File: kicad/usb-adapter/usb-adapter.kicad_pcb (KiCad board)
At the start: 2 copper layers, 17.2 x 40 mm, 3 parts, among them J1 USB-A plug, port A, J2 USB-A plug, port B, J3 To main board

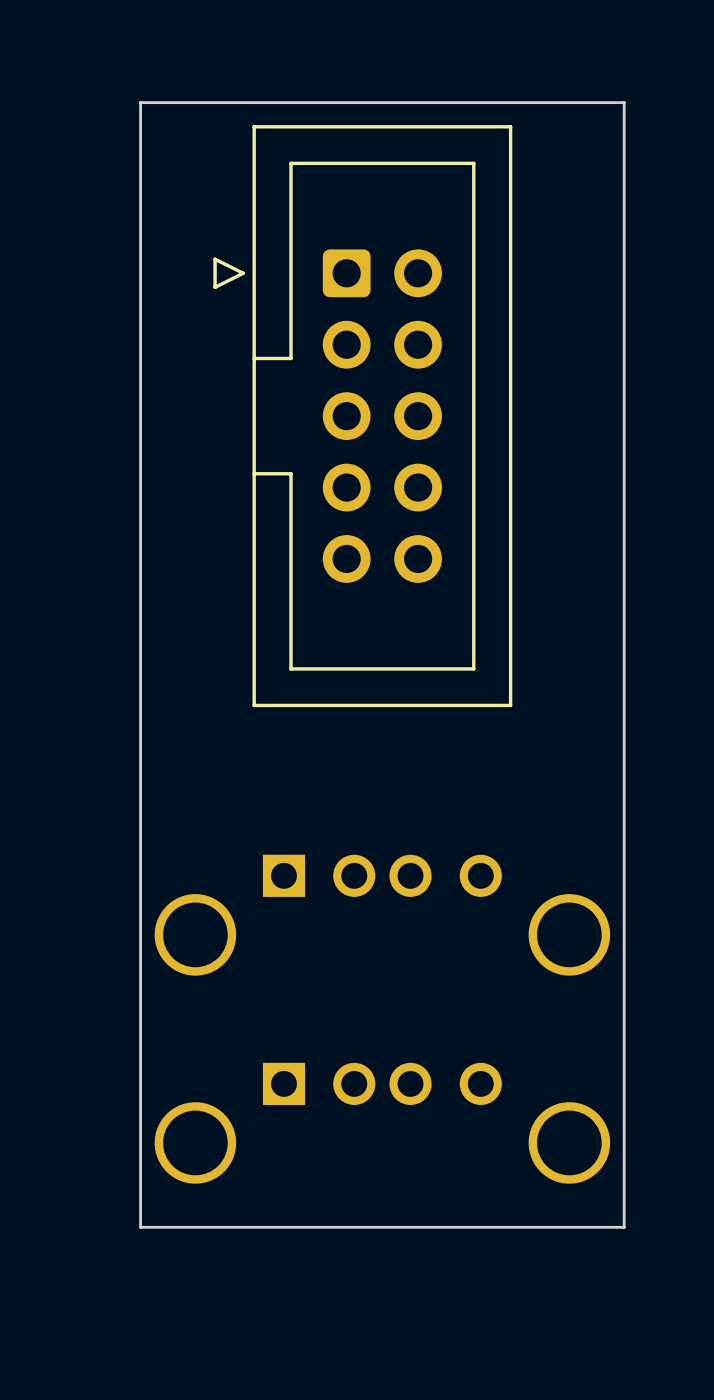
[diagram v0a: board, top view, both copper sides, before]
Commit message: USB adapter: port heights from the Pi 4 model (3.49 / 12.63 above its PCB)
Co-Authored-By: Claude Opus 5.5 <noreply@anthropic.com>
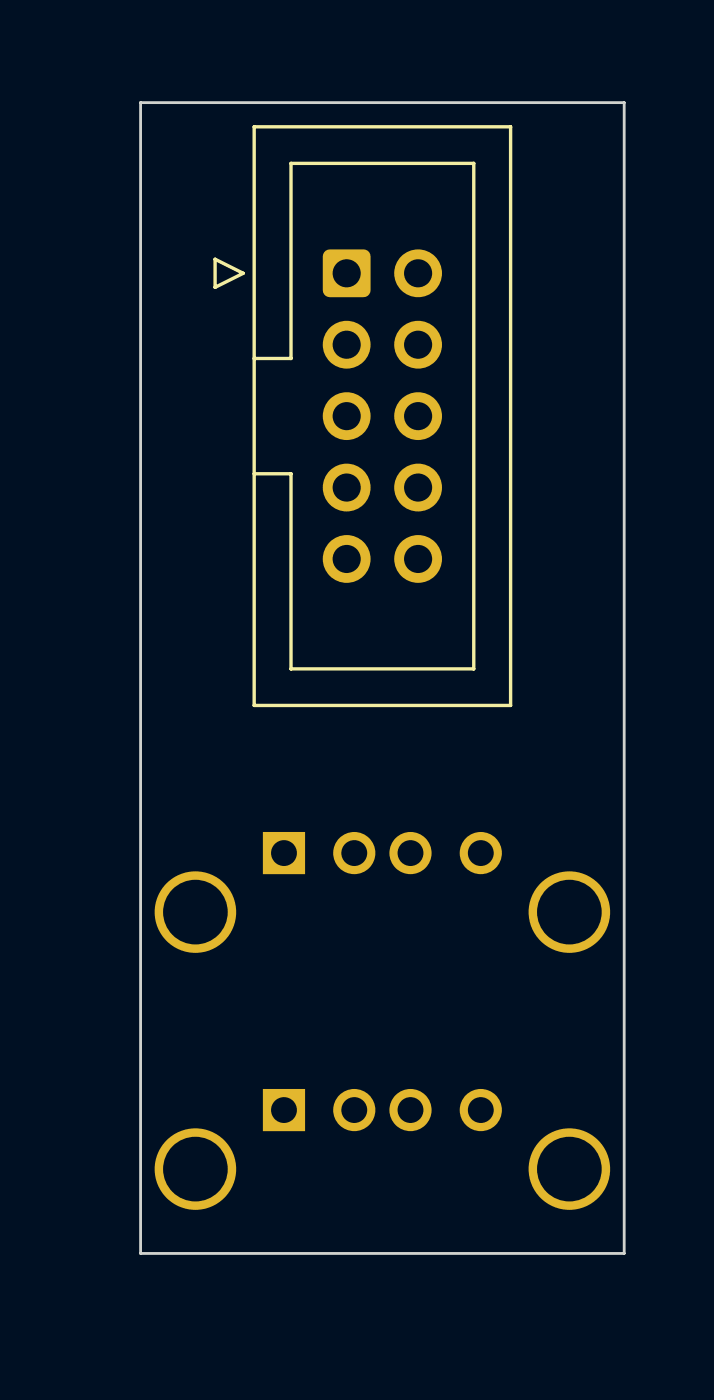
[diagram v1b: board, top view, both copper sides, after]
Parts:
- moved J2 0.93 mm to (100.0, 92.6)
- moved J1 0.81 mm to (100.0, 83.5)
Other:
- board size 17.2 x 40 mm -> 17.2 x 40.9 mm
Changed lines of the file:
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@@
 	(footprint "USB_A_Plug_Vertical"
 		(layer "F.Cu")
-		(at 100 84.3)
+		(at 100 92.63)
+		(descr "USB-A male plug, vertical (180 deg), through hole. PLACEHOLDER: common pattern, redraw from the chosen part")
+		(property "Reference" "J2"
+			(at 0 -4.5 0)
+			(layer "F.SilkS")
+			(hide yes)
+			(effects
+				(font
+					(size 1 1)
+					(thickness 0.15)
+				)
+			)
+		)
+		(property "Value" "USB-A plug, port B"
+			(at 0 5.5 0)
+			(layer "F.Fab")
+			(effects
+				(font
+					(size 1 1)
+					(thickness 0.15)
+				)
+			)
+		)
+		(property "Datasheet" ""
+			(at 0 0 0)
+			(layer "F.Fab")
+			(hide yes)
+			(effects
+				(font
+					(size 1.27 1.27)
+				)
+			)
+		)
+		(property "Description" ""
+			(at 0 0 0)
+			(layer "F.Fab")
+			(hide yes)
+			(effects
+				(font
+					(size 1.27 1.27)
+				)
+			)
+		)
+		(attr through_hole)
+		(duplicate_pad_numbers_are_jumpers no)
+		(fp_rect
+			(start -8.4 -2.75)
+			(end 8.4 2.75)
+			(stroke
+				(width 0.05)
+				(type solid)
+			)
+			(fill no)
+			(layer "F.CrtYd")
+		)
+		(fp_rect
+			(start -6 -2.25)
+			(end 6 2.25)
+			(stroke
+				(width 0.12)
+				(type solid)
+			)
+			(fill no)
+			(layer "F.Fab")
+		)
+		(pad "1" thru_hole rect
+			(at -3.5 -2.1)
+			(size 1.5 1.5)
+			(drill 0.92)
+			(layers "*.Cu" "*.Mask")
+			(remove_unused_layers no)
+			(net "VBUS_B")
+		)
+		(pad "2" thru_hole circle
+			(at -1 -2.1)
+			(size 1.5 1.5)
+			(drill 0.92)
+			(layers "*.Cu" "*.Mask")
+			(remove_unused_layers no)
+			(net "DM_B")
+		)
+		(pad "3" thru_hole circle
+			(at 1 -2.1)
+			(size 1.5 1.5)
+			(drill 0.92)
+			(layers "*.Cu" "*.Mask")
+			(remove_unused_layers no)
+			(net "DP_B")
+		)
+		(pad "4" thru_hole circle
+			(at 3.5 -2.1)
+			(size 1.5 1.5)
+			(drill 0.92)
+			(layers "*.Cu" "*.Mask")
+			(remove_unused_layers no)
+			(net "GND")
+		)
+		(pad "SH" thru_hole circle
+			(at -6.65 0)
+			(size 2.9 2.9)
+			(drill 2.3)
+			(layers "*.Cu" "*.Mask")
+			(remove_unused_layers no)
+			(net "GND")
+		)
+		(pad "SH" thru_hole circle
+			(at 6.65 0)
+			(size 2.9 2.9)
+			(drill 2.3)
+			(layers "*.Cu" "*.Mask")
+			(remove_unused_layers no)
+			(net "GND")
+		)
+		(embedded_fonts no)
+	)
+	(footprint "USB_A_Plug_Vertical"
+		(layer "F.Cu")
+		(at 100 83.49)
 		(descr "USB-A male plug, vertical (180 deg), through hole. PLACEHOLDER: common pattern, redraw from the chosen part")
 		(property "Reference" "J1"
@@
 		)
 	)
-	(footprint "USB_A_Plug_Vertical"
-		(layer "F.Cu")
-		(at 100 91.7)
-		(descr "USB-A male plug, vertical (180 deg), through hole. PLACEHOLDER: common pattern, redraw from the chosen part")
-		(property "Reference" "J2"
-			(at 0 -4.5 0)
-			(layer "F.SilkS")
-			(hide yes)
-			(effects
-				(font
-					(size 1 1)
-					(thickness 0.15)
-				)
-			)
-		)
-		(property "Value" "USB-A plug, port B"
-			(at 0 5.5 0)
-			(layer "F.Fab")
-			(effects
-				(font
-					(size 1 1)
-					(thickness 0.15)
-				)
-			)
-		)
-		(property "Datasheet" ""
-			(at 0 0 0)
-			(layer "F.Fab")
-			(hide yes)
-			(effects
-				(font
-					(size 1.27 1.27)
-				)
-			)
-		)
-		(property "Description" ""
-			(at 0 0 0)
-			(layer "F.Fab")
-			(hide yes)
-			(effects
-				(font
-					(size 1.27 1.27)
-				)
-			)
-		)
-		(attr through_hole)
-		(duplicate_pad_numbers_are_jumpers no)
-		(fp_rect
-			(start -8.4 -2.75)
-			(end 8.4 2.75)
-			(stroke
-				(width 0.05)
-				(type solid)
-			)
-			(fill no)
-			(layer "F.CrtYd")
-		)
-		(fp_rect
-			(start -6 -2.25)
-			(end 6 2.25)
-			(stroke
-				(width 0.12)
-				(type solid)
-			)
-			(fill no)
-			(layer "F.Fab")
-		)
-		(pad "1" thru_hole rect
-			(at -3.5 -2.1)
-			(size 1.5 1.5)
-			(drill 0.92)
-			(layers "*.Cu" "*.Mask")
-			(remove_unused_layers no)
-			(net "VBUS_B")
-		)
-		(pad "2" thru_hole circle
-			(at -1 -2.1)
-			(size 1.5 1.5)
-			(drill 0.92)
-			(layers "*.Cu" "*.Mask")
-			(remove_unused_layers no)
-			(net "DM_B")
-		)
-		(pad "3" thru_hole circle
-			(at 1 -2.1)
-			(size 1.5 1.5)
-			(drill 0.92)
-			(layers "*.Cu" "*.Mask")
-			(remove_unused_layers no)
-			(net "DP_B")
-		)
-		(pad "4" thru_hole circle
-			(at 3.5 -2.1)
-			(size 1.5 1.5)
-			(drill 0.92)
-			(layers "*.Cu" "*.Mask")
-			(remove_unused_layers no)
-			(net "GND")
-		)
-		(pad "SH" thru_hole circle
-			(at -6.65 0)
-			(size 2.9 2.9)
-			(drill 2.3)
-			(layers "*.Cu" "*.Mask")
-			(remove_unused_layers no)
-			(net "GND")
-		)
-		(pad "SH" thru_hole circle
-			(at 6.65 0)
-			(size 2.9 2.9)
-			(drill 2.3)
-			(layers "*.Cu" "*.Mask")
-			(remove_unused_layers no)
-			(net "GND")
-		)
-		(embedded_fonts no)
-	)
 	(gr_line
 		(start 88.4 76.6)
@@
 	(gr_rect
 		(start 91.4 54.7)
-		(end 108.6 94.7)
+		(end 108.6 95.63)
 		(radius 1)
 		(stroke

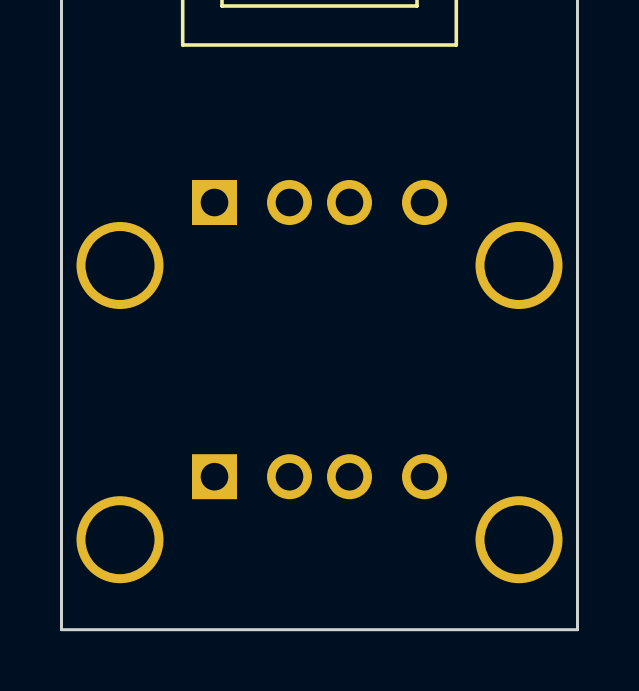
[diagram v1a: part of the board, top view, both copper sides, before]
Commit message: USB adapter: footprint for the USB-71 side-mount plug stood on end
Tails straight through in plated slots at the side-mount spacing, shell
tabs in slots at the jack's edges, insert toward the Pi's PCB. The board
now links to the schematic (footprint ids, symbol paths, net names), so
Update PCB leaves it alone.

Co-Authored-By: Claude Opus 5.5 <noreply@anthropic.com>
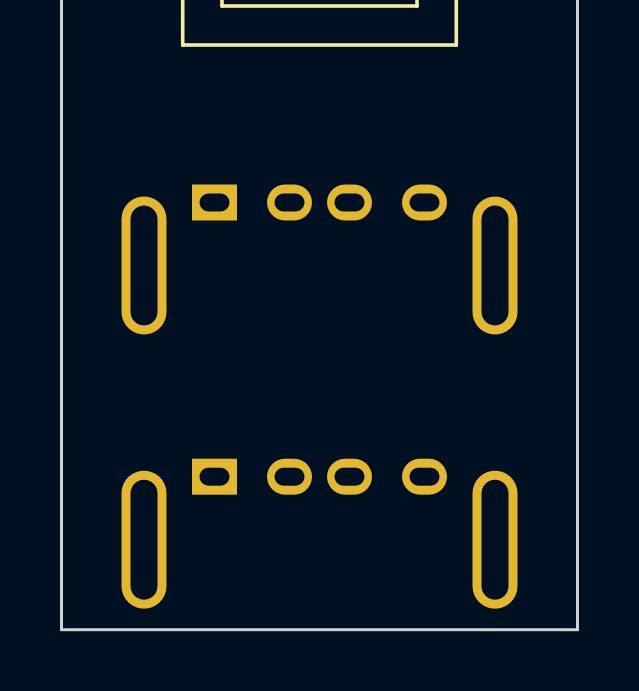
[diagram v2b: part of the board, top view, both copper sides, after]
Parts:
- J1, J2: footprint USB_A_Plug_Vertical -> usb-adapter:USB_A_Plug_Vertical
- J3: footprint IDC-Header_2x05_P2.54mm_Vertical -> Connector_IDC:IDC-Header_2x05_P2.54mm_Vertical
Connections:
- net DM_A renamed /DM_A
- net DM_B renamed /DM_B
- net DP_A renamed /DP_A
- net DP_B renamed /DP_B
- net VBUS_A renamed /VBUS_A
- net VBUS_B renamed /VBUS_B
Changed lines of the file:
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@@
 		)
 	)
-	(footprint "USB_A_Plug_Vertical"
+	(footprint "usb-adapter:USB_A_Plug_Vertical"
 		(layer "F.Cu")
-		(at 100 92.63)
-		(descr "USB-A male plug, vertical (180 deg), through hole. PLACEHOLDER: common pattern, redraw from the chosen part")
-		(property "Reference" "J2"
+		(at 100 83.49)
+		(descr "USB-A male plug, side-mount USB-71 type (L 15 mm, Molex 48037 pattern) stood on its back end: tails straight through in slots, shell tabs in slots at the jack edges")
+		(property "Reference" "J1"
 			(at 0 -4.5 0)
 			(layer "F.SilkS")
@@
 			)
 		)
-		(property "Value" "USB-A plug, port B"
-			(at 0 5.5 0)
+		(property "Value" "USB-A plug, port A"
+			(at 0 4 0)
 			(layer "F.Fab")
 			(effects
@@
 			)
 		)
+		(sheetname "/")
+		(sheetfile "usb-adapter.kicad_sch")
 		(attr through_hole)
 		(duplicate_pad_numbers_are_jumpers no)
 		(fp_rect
-			(start -8.4 -2.75)
-			(end 8.4 2.75)
+			(start -7 -3)
+			(end 7 3)
 			(stroke
 				(width 0.05)
@@
 			(fill no)
 			(layer "F.CrtYd")
+		)
+		(fp_line
+			(start -4.5 -1.65)
+			(end 4.5 -1.65)
+			(stroke
+				(width 0.1)
+				(type solid)
+			)
+			(layer "F.Fab")
 		)
 		(fp_rect
@@
 			(end 6 2.25)
 			(stroke
-				(width 0.12)
+				(width 0.1)
 				(type solid)
 			)
 			(fill no)
 			(layer "F.Fab")
+		)
+		(fp_text user "insert"
+			(at 0 -0.85 0)
+			(layer "F.Fab")
+			(effects
+				(font
+					(size 0.6 0.6)
+					(thickness 0.08)
+				)
+			)
 		)
 		(pad "1" thru_hole rect
 			(at -3.5 -2.1)
-			(size 1.5 1.5)
-			(drill 0.92)
-			(layers "*.Cu" "*.Mask")
-			(remove_unused_layers no)
-			(net "VBUS_B")
-		)
-		(pad "2" thru_hole circle
+			(size 1.5 1.2)
+			(drill oval 1 0.6)
+			(layers "*.Cu" "*.Mask")
+			(remove_unused_layers no)
+			(net "/VBUS_A")
+		)
+		(pad "2" thru_hole oval
 			(at -1 -2.1)
-			(size 1.5 1.5)
-			(drill 0.92)
-			(layers "*.Cu" "*.Mask")
-			(remove_unused_layers no)
-			(net "DM_B")
-		)
-		(pad "3" thru_hole circle
+			(size 1.5 1.2)
+			(drill oval 1 0.6)
+			(layers "*.Cu" "*.Mask")
+			(remove_unused_layers no)
+			(net "/DM_A")
+		)
+		(pad "3" thru_hole oval
 			(at 1 -2.1)
-			(size 1.5 1.5)
-			(drill 0.92)
-			(layers "*.Cu" "*.Mask")
-			(remove_unused_layers no)
-			(net "DP_B")
-		)
-		(pad "4" thru_hole circle
+			(size 1.5 1.2)
+			(drill oval 1 0.6)
+			(layers "*.Cu" "*.Mask")
+			(remove_unused_layers no)
+			(net "/DP_A")
+		)
+		(pad "4" thru_hole oval
 			(at 3.5 -2.1)
-			(size 1.5 1.5)
-			(drill 0.92)
-			(layers "*.Cu" "*.Mask")
-			(remove_unused_layers no)
-			(net "GND")
-		)
-		(pad "SH" thru_hole circle
-			(at -6.65 0)
-			(size 2.9 2.9)
-			(drill 2.3)
-			(layers "*.Cu" "*.Mask")
-			(remove_unused_layers no)
-			(net "GND")
-		)
-		(pad "SH" thru_hole circle
-			(at 6.65 0)
-			(size 2.9 2.9)
-			(drill 2.3)
+			(size 1.5 1.2)
+			(drill oval 1 0.6)
+			(layers "*.Cu" "*.Mask")
+			(remove_unused_layers no)
+			(net "GND")
+		)
+		(pad "SH" thru_hole oval
+			(at -5.85 0)
+			(size 1.5 4.6)
+			(drill oval 0.9 4)
+			(layers "*.Cu" "*.Mask")
+			(remove_unused_layers no)
+			(net "GND")
+		)
+		(pad "SH" thru_hole oval
+			(at 5.85 0)
+			(size 1.5 4.6)
+			(drill oval 0.9 4)
 			(layers "*.Cu" "*.Mask")
 			(remove_unused_layers no)
@@
 		(embedded_fonts no)
 	)
-	(footprint "USB_A_Plug_Vertical"
-		(layer "F.Cu")
-		(at 100 83.49)
-		(descr "USB-A male plug, vertical (180 deg), through hole. PLACEHOLDER: common pattern, redraw from the chosen part")
-		(property "Reference" "J1"
-			(at 0 -4.5 0)
-			(layer "F.SilkS")
-			(hide yes)
-			(effects
-				(font
-					(size 1 1)
-					(thickness 0.15)
-				)
-			)
-		)
-		(property "Value" "USB-A plug, port A"
-			(at 0 5.5 0)
-			(layer "F.Fab")
-			(effects
-				(font
-					(size 1 1)
-					(thickness 0.15)
-				)
-			)
-		)
-		(property "Datasheet" ""
-			(at 0 0 0)
-			(layer "F.Fab")
-			(hide yes)
-			(effects
-				(font
-					(size 1.27 1.27)
-				)
-			)
-		)
-		(property "Description" ""
-			(at 0 0 0)
-			(layer "F.Fab")
-			(hide yes)
-			(effects
-				(font
-					(size 1.27 1.27)
-				)
-			)
-		)
-		(attr through_hole)
-		(duplicate_pad_numbers_are_jumpers no)
-		(fp_rect
-			(start -8.4 -2.75)
-			(end 8.4 2.75)
-			(stroke
-				(width 0.05)
-				(type solid)
-			)
-			(fill no)
-			(layer "F.CrtYd")
-		)
-		(fp_rect
-			(start -6 -2.25)
-			(end 6 2.25)
-			(stroke
-				(width 0.12)
-				(type solid)
-			)
-			(fill no)
-			(layer "F.Fab")
-		)
-		(pad "1" thru_hole rect
-			(at -3.5 -2.1)
-			(size 1.5 1.5)
-			(drill 0.92)
-			(layers "*.Cu" "*.Mask")
-			(remove_unused_layers no)
-			(net "VBUS_A")
-		)
-		(pad "2" thru_hole circle
-			(at -1 -2.1)
-			(size 1.5 1.5)
-			(drill 0.92)
-			(layers "*.Cu" "*.Mask")
-			(remove_unused_layers no)
-			(net "DM_A")
-		)
-		(pad "3" thru_hole circle
-			(at 1 -2.1)
-			(size 1.5 1.5)
-			(drill 0.92)
-			(layers "*.Cu" "*.Mask")
-			(remove_unused_layers no)
-			(net "DP_A")
-		)
-		(pad "4" thru_hole circle
-			(at 3.5 -2.1)
-			(size 1.5 1.5)
-			(drill 0.92)
-			(layers "*.Cu" "*.Mask")
-			(remove_unused_layers no)
-			(net "GND")
-		)
-		(pad "SH" thru_hole circle
-			(at -6.65 0)
-			(size 2.9 2.9)
-			(drill 2.3)
-			(layers "*.Cu" "*.Mask")
-			(remove_unused_layers no)
-			(net "GND")
-		)
-		(pad "SH" thru_hole circle
-			(at 6.65 0)
-			(size 2.9 2.9)
-			(drill 2.3)
-			(layers "*.Cu" "*.Mask")
-			(remove_unused_layers no)
-			(net "GND")
-		)
-		(embedded_fonts no)
-	)
-	(footprint "IDC-Header_2x05_P2.54mm_Vertical"
+	(footprint "Connector_IDC:IDC-Header_2x05_P2.54mm_Vertical"
 		(layer "F.Cu")
 		(at 98.73 60.769999)
@@
 			)
 		)
+		(sheetname "/")
+		(sheetfile "usb-adapter.kicad_sch")
 		(attr through_hole)
 		(duplicate_pad_numbers_are_jumpers no)
@@
 			(remove_unused_layers no)
 			(roundrect_rratio 0.147059)
-			(net "VBUS_A")
+			(net "/VBUS_A")
 		)
 		(pad "2" thru_hole circle
@@
 			(layers "*.Cu" "*.Mask")
 			(remove_unused_layers no)
-			(net "DM_A")
+			(net "/DM_A")
 		)
 		(pad "4" thru_hole circle
@@
 			(layers "*.Cu" "*.Mask")
 			(remove_unused_layers no)
-			(net "DP_A")
+			(net "/DP_A")
 		)
 		(pad "5" thru_hole circle
@@
 			(layers "*.Cu" "*.Mask")
 			(remove_unused_layers no)
-			(net "DM_B")
+			(net "/DM_B")
 		)
 		(pad "8" thru_hole circle
@@
 			(layers "*.Cu" "*.Mask")
 			(remove_unused_layers no)
-			(net "DP_B")
+			(net "/DP_B")
 		)
 		(pad "9" thru_hole circle
@@
 			(layers "*.Cu" "*.Mask")
 			(remove_unused_layers no)
-			(net "VBUS_B")
+			(net "/VBUS_B")
 		)
 		(embedded_fonts no)
@@
 		)
 	)
+	(footprint "usb-adapter:USB_A_Plug_Vertical"
+		(layer "F.Cu")
+		(at 100 92.63)
+		(descr "USB-A male plug, side-mount USB-71 type (L 15 mm, Molex 48037 pattern) stood on its back end: tails straight through in slots, shell tabs in slots at the jack edges")
+		(property "Reference" "J2"
+			(at 0 -4.5 0)
+			(layer "F.SilkS")
+			(hide yes)
+			(effects
+				(font
+					(size 1 1)
+					(thickness 0.15)
+				)
+			)
+		)
+		(property "Value" "USB-A plug, port B"
+			(at 0 4 0)
+			(layer "F.Fab")
+			(effects
+				(font
+					(size 1 1)
+					(thickness 0.15)
+				)
+			)
+		)
+		(property "Datasheet" ""
+			(at 0 0 0)
+			(layer "F.Fab")
+			(hide yes)
+			(effects
+				(font
+					(size 1.27 1.27)
+				)
+			)
+		)
+		(property "Description" ""
+			(at 0 0 0)
+			(layer "F.Fab")
+			(hide yes)
+			(effects
+				(font
+					(size 1.27 1.27)
+				)
+			)
+		)
+		(sheetname "/")
+		(sheetfile "usb-adapter.kicad_sch")
+		(attr through_hole)
+		(duplicate_pad_numbers_are_jumpers no)
+		(fp_rect
+			(start -7 -3)
+			(end 7 3)
+			(stroke
+				(width 0.05)
+				(type solid)
+			)
+			(fill no)
+			(layer "F.CrtYd")
+		)
+		(fp_line
+			(start -4.5 -1.65)
+			(end 4.5 -1.65)
+			(stroke
+				(width 0.1)
+				(type solid)
+			)
+			(layer "F.Fab")
+		)
+		(fp_rect
+			(start -6 -2.25)
+			(end 6 2.25)
+			(stroke
+				(width 0.1)
+				(type solid)
+			)
+			(fill no)
+			(layer "F.Fab")
+		)
+		(fp_text user "insert"
+			(at 0 -0.85 0)
+			(layer "F.Fab")
+			(effects
+				(font
+					(size 0.6 0.6)
+					(thickness 0.08)
+				)
+			)
+		)
+		(pad "1" thru_hole rect
+			(at -3.5 -2.1)
+			(size 1.5 1.2)
+			(drill oval 1 0.6)
+			(layers "*.Cu" "*.Mask")
+			(remove_unused_layers no)
+			(net "/VBUS_B")
+		)
+		(pad "2" thru_hole oval
+			(at -1 -2.1)
+			(size 1.5 1.2)
+			(drill oval 1 0.6)
+			(layers "*.Cu" "*.Mask")
+			(remove_unused_layers no)
+			(net "/DM_B")
+		)
+		(pad "3" thru_hole oval
+			(at 1 -2.1)
+			(size 1.5 1.2)
+			(drill oval 1 0.6)
+			(layers "*.Cu" "*.Mask")
+			(remove_unused_layers no)
+			(net "/DP_B")
+		)
+		(pad "4" thru_hole oval
+			(at 3.5 -2.1)
+			(size 1.5 1.2)
+			(drill oval 1 0.6)
+			(layers "*.Cu" "*.Mask")
+			(remove_unused_layers no)
+			(net "GND")
+		)
+		(pad "SH" thru_hole oval
+			(at -5.85 0)
+			(size 1.5 4.6)
+			(drill oval 0.9 4)
+			(layers "*.Cu" "*.Mask")
+			(remove_unused_layers no)
+			(net "GND")
+		)
+		(pad "SH" thru_hole oval
+			(at 5.85 0)
+			(size 1.5 4.6)
+			(drill oval 0.9 4)
+			(layers "*.Cu" "*.Mask")
+			(remove_unused_layers no)
+			(net "GND")
+		)
+		(embedded_fonts no)
+	)
 	(gr_line
